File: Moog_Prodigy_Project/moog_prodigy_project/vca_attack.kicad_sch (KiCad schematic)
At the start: 14 parts, among them U105 MC14007UBCP, U106 MC14007UBCP, U107 MC14007UBCP

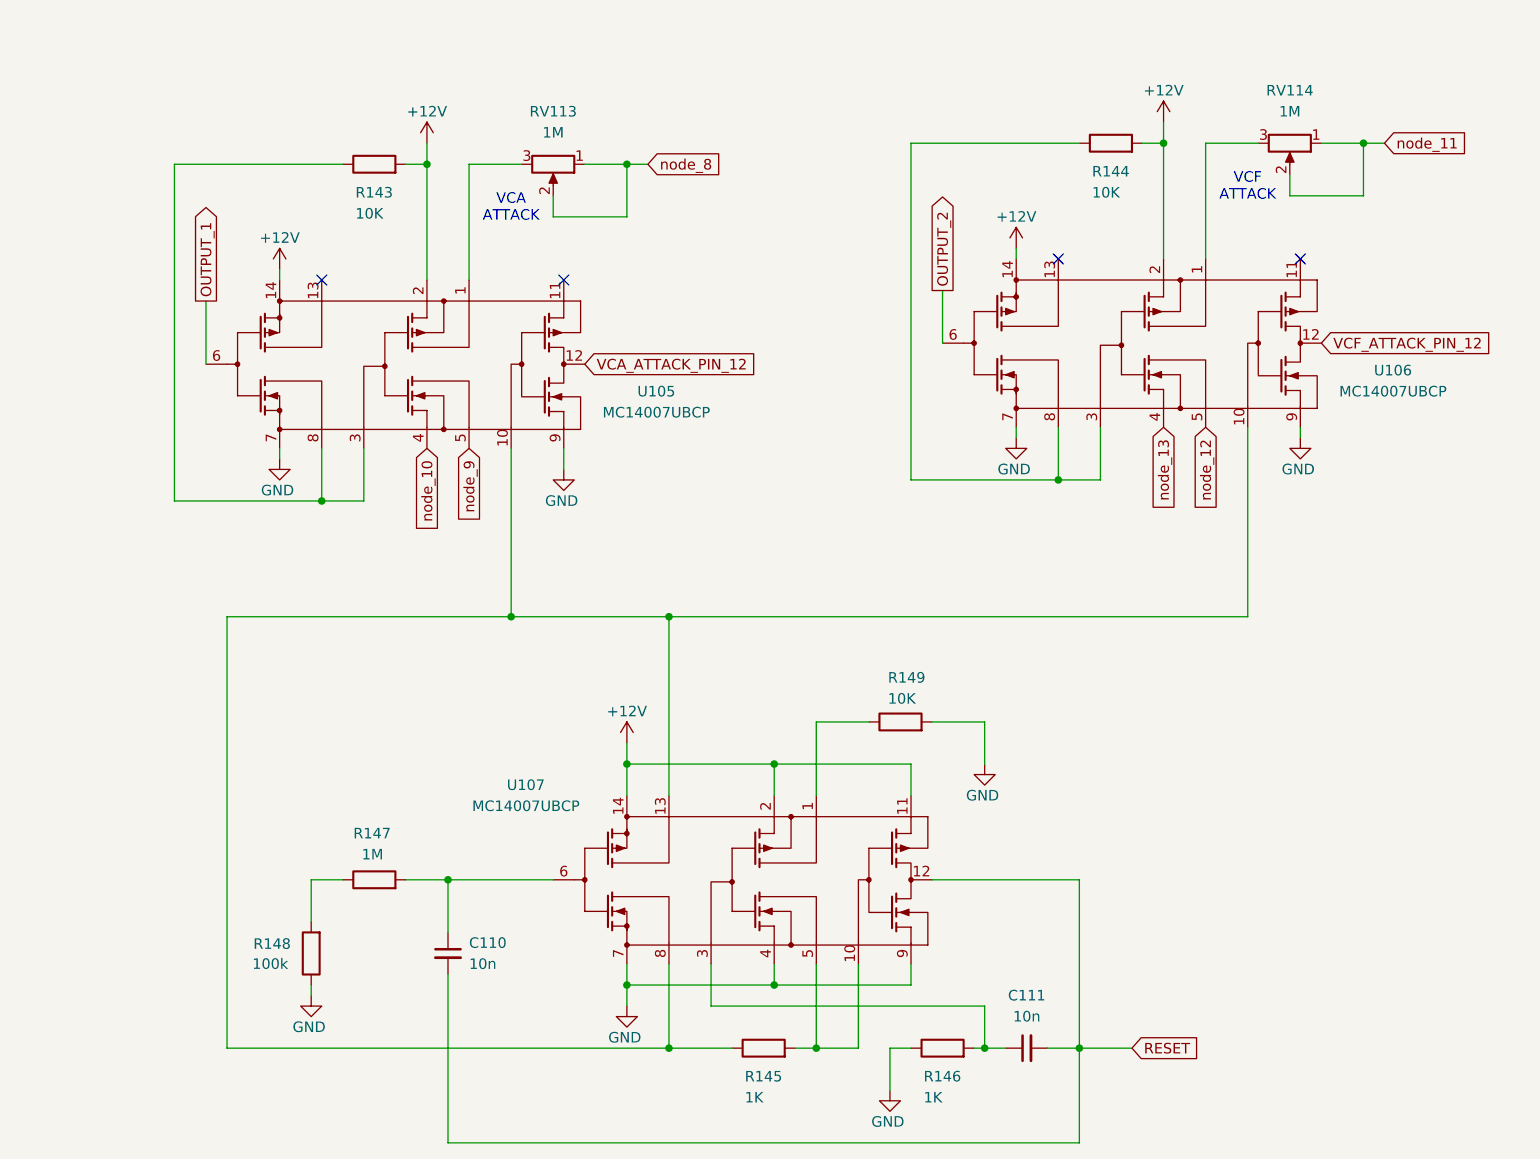
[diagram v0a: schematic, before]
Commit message: problemi sa ca3096, multiplicirani footprintovi
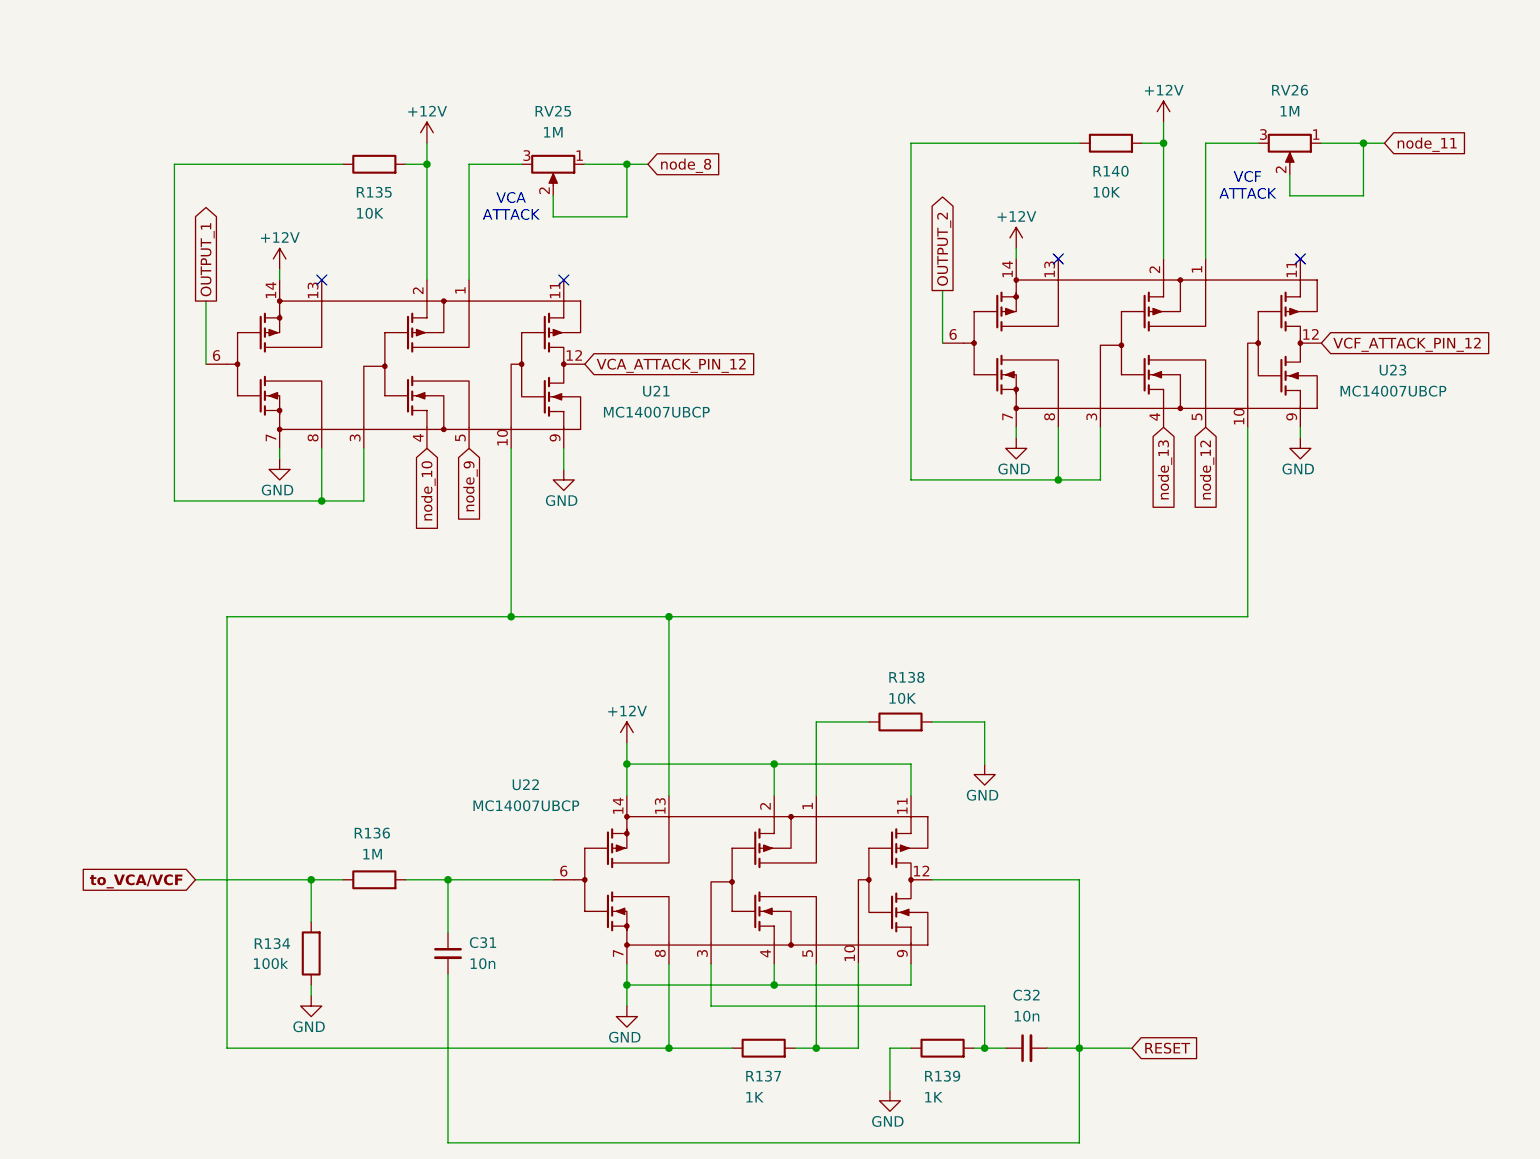
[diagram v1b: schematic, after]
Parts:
- renumbered C110 to C31, C111 to C32, R148 to R134, R143 to R135, R147 to R136, R145 to R137, R149 to R138, R146 to R139, R144 to R140, RV113 to RV25, RV114 to RV26, U105 to U21, U107 to U22, U106 to U23
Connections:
- net to_VCA/VCF: now reaches R134.2, R136.1
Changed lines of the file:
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@@
+	)
+	(junction
+		(at 74.93 125.73)
+		(diameter 0)
+		(color 0 0 0 0)
 	)
 	(junction
@@
 		(pts
 			(xy 156.21 111.76) (xy 156.21 106.68)
+		)
+		(stroke
+			(width 0)
+			(type default)
+		)
+	)
+	(wire
+		(pts
+			(xy 60.96 125.73) (xy 74.93 125.73)
 		)
 		(stroke
@@
 				)
 				(justify left)
+				(hide yes)
+			)
+		)
+	)
+	(global_label "to_VCA{slash}VCF"
+		(shape input)
+		(at 60.96 125.73 180)
+		(fields_autoplaced yes)
+		(effects
+			(font
+				(size 1.27 1.27)
+				(thickness 0.254)
+				(bold yes)
+			)
+			(justify right)
+		)
+		(property "Intersheetrefs" "${INTERSHEET_REFS}"
+			(at 46.4316 125.73 0)
+			(effects
+				(font
+					(size 1.27 1.27)
+				)
+				(justify right)
 				(hide yes)
 			)
@@
 		(on_board yes)
 		(dnp no)
-		(property "Reference" "R149"
+		(property "Reference" "R138"
 			(at 144.526 101.346 90)
 			(effects
@@
 			(project "moog_prodigy_project"
 				(path "/db469bdb-b6c3-4a16-9199-d4e6b8d556e8/f72090f0-21a5-4951-9fe6-dcdfafa76d53"
-					(reference "R149")
+					(reference "R138")
 					(unit 1)
 				)
@@
 		(on_board yes)
 		(dnp no)
-		(property "Reference" "R146"
+		(property "Reference" "R139"
 			(at 148.844 149.479 90)
 			(effects
@@
 			(project "moog_prodigy_project"
 				(path "/db469bdb-b6c3-4a16-9199-d4e6b8d556e8/f72090f0-21a5-4951-9fe6-dcdfafa76d53"
-					(reference "R146")
+					(reference "R139")
 					(unit 1)
 				)
@@
 		(on_board yes)
 		(dnp no)
-		(property "Reference" "#PWR0154"
+		(property "Reference" "#PWR0164"
 			(at 74.93 146.05 0)
 			(effects
@@
 			(project "moog_prodigy_project"
 				(path "/db469bdb-b6c3-4a16-9199-d4e6b8d556e8/f72090f0-21a5-4951-9fe6-dcdfafa76d53"
-					(reference "#PWR0154")
+					(reference "#PWR0164")
 					(unit 1)
 				)
@@
 		(on_board yes)
 		(dnp no)
-		(property "Reference" "U107"
+		(property "Reference" "U22"
 			(at 100.838 114.3 0)
 			(effects
@@
 			(project "moog_prodigy_project"
 				(path "/db469bdb-b6c3-4a16-9199-d4e6b8d556e8/f72090f0-21a5-4951-9fe6-dcdfafa76d53"
-					(reference "U107")
+					(reference "U22")
 					(unit 1)
 				)
@@
 		(on_board yes)
 		(dnp no)
-		(property "Reference" "#PWR0147"
+		(property "Reference" "#PWR0165"
 			(at 88.9 40.64 0)
 			(effects
@@
 			(project "moog_prodigy_project"
 				(path "/db469bdb-b6c3-4a16-9199-d4e6b8d556e8/f72090f0-21a5-4951-9fe6-dcdfafa76d53"
-					(reference "#PWR0147")
+					(reference "#PWR0165")
 					(unit 1)
 				)
@@
 		(on_board yes)
 		(dnp no)
-		(property "Reference" "R145"
+		(property "Reference" "R137"
 			(at 127.254 149.479 90)
 			(effects
@@
 			(project "moog_prodigy_project"
 				(path "/db469bdb-b6c3-4a16-9199-d4e6b8d556e8/f72090f0-21a5-4951-9fe6-dcdfafa76d53"
-					(reference "R145")
+					(reference "R137")
 					(unit 1)
 				)
@@
 		(on_board yes)
 		(dnp no)
-		(property "Reference" "#PWR0157"
+		(property "Reference" "#PWR0168"
 			(at 113.03 147.32 0)
 			(effects
@@
 			(project "moog_prodigy_project"
 				(path "/db469bdb-b6c3-4a16-9199-d4e6b8d556e8/f72090f0-21a5-4951-9fe6-dcdfafa76d53"
-					(reference "#PWR0157")
+					(reference "#PWR0168")
 					(unit 1)
 				)
@@
 		(on_board yes)
 		(dnp no)
-		(property "Reference" "R144"
+		(property "Reference" "R140"
 			(at 169.164 40.259 90)
 			(effects
@@
 			(project "moog_prodigy_project"
 				(path "/db469bdb-b6c3-4a16-9199-d4e6b8d556e8/f72090f0-21a5-4951-9fe6-dcdfafa76d53"
-					(reference "R144")
+					(reference "R140")
 					(unit 1)
 				)
@@
 		(dnp no)
 		(fields_autoplaced yes)
-		(property "Reference" "RV114"
+		(property "Reference" "RV26"
 			(at 193.04 30.48 90)
 			(effects
@@
 			(project "moog_prodigy_project"
 				(path "/db469bdb-b6c3-4a16-9199-d4e6b8d556e8/f72090f0-21a5-4951-9fe6-dcdfafa76d53"
-					(reference "RV114")
+					(reference "RV26")
 					(unit 1)
 				)
@@
 		(on_board yes)
 		(dnp no)
-		(property "Reference" "#PWR0152"
+		(property "Reference" "#PWR0172"
 			(at 160.02 78.74 0)
 			(effects
@@
 			(project "moog_prodigy_project"
 				(path "/db469bdb-b6c3-4a16-9199-d4e6b8d556e8/f72090f0-21a5-4951-9fe6-dcdfafa76d53"
-					(reference "#PWR0152")
+					(reference "#PWR0172")
 					(unit 1)
 				)
@@
 		(on_board yes)
 		(dnp no)
-		(property "Reference" "U105"
+		(property "Reference" "U21"
 			(at 116.586 66.802 0)
 			(effects
@@
 			(project "moog_prodigy_project"
 				(path "/db469bdb-b6c3-4a16-9199-d4e6b8d556e8/f72090f0-21a5-4951-9fe6-dcdfafa76d53"
-					(reference "U105")
+					(reference "U21")
 					(unit 1)
 				)
@@
 		(on_board yes)
 		(dnp no)
-		(property "Reference" "R147"
+		(property "Reference" "R136"
 			(at 80.01 120.142 90)
 			(effects
@@
 			(project "moog_prodigy_project"
 				(path "/db469bdb-b6c3-4a16-9199-d4e6b8d556e8/f72090f0-21a5-4951-9fe6-dcdfafa76d53"
-					(reference "R147")
+					(reference "R136")
 					(unit 1)
 				)
@@
 		(on_board yes)
 		(dnp no)
-		(property "Reference" "#PWR0151"
+		(property "Reference" "#PWR0166"
 			(at 105.41 82.55 0)
 			(effects
@@
 			(project "moog_prodigy_project"
 				(path "/db469bdb-b6c3-4a16-9199-d4e6b8d556e8/f72090f0-21a5-4951-9fe6-dcdfafa76d53"
-					(reference "#PWR0151")
+					(reference "#PWR0166")
 					(unit 1)
 				)
@@
 		(on_board yes)
 		(dnp no)
-		(property "Reference" "#PWR0155"
+		(property "Reference" "#PWR0167"
 			(at 113.03 113.03 0)
 			(effects
@@
 			(project "moog_prodigy_project"
 				(path "/db469bdb-b6c3-4a16-9199-d4e6b8d556e8/f72090f0-21a5-4951-9fe6-dcdfafa76d53"
-					(reference "#PWR0155")
+					(reference "#PWR0167")
 					(unit 1)
 				)
@@
 		(on_board yes)
 		(dnp no)
-		(property "Reference" "R143"
+		(property "Reference" "R135"
 			(at 80.264 42.799 90)
 			(effects
@@
 			(project "moog_prodigy_project"
 				(path "/db469bdb-b6c3-4a16-9199-d4e6b8d556e8/f72090f0-21a5-4951-9fe6-dcdfafa76d53"
-					(reference "R143")
+					(reference "R135")
 					(unit 1)
 				)
@@
 		(dnp no)
 		(fields_autoplaced yes)
-		(property "Reference" "C111"
+		(property "Reference" "C32"
 			(at 161.2963 139.7 90)
 			(effects
@@
 			(project "moog_prodigy_project"
 				(path "/db469bdb-b6c3-4a16-9199-d4e6b8d556e8/f72090f0-21a5-4951-9fe6-dcdfafa76d53"
-					(reference "C111")
+					(reference "C32")
 					(unit 1)
 				)
@@
 		(dnp no)
 		(fields_autoplaced yes)
-		(property "Reference" "RV113"
+		(property "Reference" "RV25"
 			(at 104.14 33.02 90)
 			(effects
@@
 			(project "moog_prodigy_project"
 				(path "/db469bdb-b6c3-4a16-9199-d4e6b8d556e8/f72090f0-21a5-4951-9fe6-dcdfafa76d53"
-					(reference "RV113")
+					(reference "RV25")
 					(unit 1)
 				)
@@
 		(on_board yes)
 		(dnp no)
-		(property "Reference" "U106"
+		(property "Reference" "U23"
 			(at 205.486 64.262 0)
 			(effects
@@
 			(project "moog_prodigy_project"
 				(path "/db469bdb-b6c3-4a16-9199-d4e6b8d556e8/f72090f0-21a5-4951-9fe6-dcdfafa76d53"
-					(reference "U106")
+					(reference "U23")
 					(unit 1)
 				)
@@
 		(on_board yes)
 		(dnp no)
-		(property "Reference" "#PWR0149"
+		(property "Reference" "#PWR0173"
 			(at 177.8 38.1 0)
 			(effects
@@
 			(project "moog_prodigy_project"
 				(path "/db469bdb-b6c3-4a16-9199-d4e6b8d556e8/f72090f0-21a5-4951-9fe6-dcdfafa76d53"
-					(reference "#PWR0149")
+					(reference "#PWR0173")
 					(unit 1)
 				)
@@
 		(on_board yes)
 		(dnp no)
-		(property "Reference" "R148"
+		(property "Reference" "R134"
 			(at 67.945 133.477 0)
 			(effects
@@
 			(project "moog_prodigy_project"
 				(path "/db469bdb-b6c3-4a16-9199-d4e6b8d556e8/f72090f0-21a5-4951-9fe6-dcdfafa76d53"
-					(reference "R148")
+					(reference "R134")
 					(unit 1)
 				)
@@
 		(on_board yes)
 		(dnp no)
-		(property "Reference" "#PWR0153"
+		(property "Reference" "#PWR0174"
 			(at 194.31 78.74 0)
 			(effects
@@
 			(project "moog_prodigy_project"
 				(path "/db469bdb-b6c3-4a16-9199-d4e6b8d556e8/f72090f0-21a5-4951-9fe6-dcdfafa76d53"
-					(reference "#PWR0153")
+					(reference "#PWR0174")
 					(unit 1)
 				)
@@
 		(on_board yes)
 		(dnp no)
-		(property "Reference" "#PWR0146"
+		(property "Reference" "#PWR0162"
 			(at 71.12 55.88 0)
 			(effects
@@
 			(project "moog_prodigy_project"
 				(path "/db469bdb-b6c3-4a16-9199-d4e6b8d556e8/f72090f0-21a5-4951-9fe6-dcdfafa76d53"
-					(reference "#PWR0146")
+					(reference "#PWR0162")
 					(unit 1)
 				)
@@
 		(on_board yes)
 		(dnp no)
-		(property "Reference" "#PWR0156"
+		(property "Reference" "#PWR0170"
 			(at 156.21 118.11 0)
 			(effects
@@
 			(project "moog_prodigy_project"
 				(path "/db469bdb-b6c3-4a16-9199-d4e6b8d556e8/f72090f0-21a5-4951-9fe6-dcdfafa76d53"
-					(reference "#PWR0156")
+					(reference "#PWR0170")
 					(unit 1)
 				)
@@
 		(on_board yes)
 		(dnp no)
-		(property "Reference" "#PWR0158"
+		(property "Reference" "#PWR0169"
 			(at 144.78 157.48 0)
 			(effects
@@
 			(project "moog_prodigy_project"
 				(path "/db469bdb-b6c3-4a16-9199-d4e6b8d556e8/f72090f0-21a5-4951-9fe6-dcdfafa76d53"
-					(reference "#PWR0158")
+					(reference "#PWR0169")
 					(unit 1)
 				)
@@
 		(dnp no)
 		(fields_autoplaced yes)
-		(property "Reference" "C110"
+		(property "Reference" "C31"
 			(at 93.98 133.3562 0)
 			(effects
@@
 			(project "moog_prodigy_project"
 				(path "/db469bdb-b6c3-4a16-9199-d4e6b8d556e8/f72090f0-21a5-4951-9fe6-dcdfafa76d53"
-					(reference "C110")
+					(reference "C31")
 					(unit 1)
 				)
@@
 		(on_board yes)
 		(dnp no)
-		(property "Reference" "#PWR0148"
+		(property "Reference" "#PWR0171"
 			(at 160.02 53.34 0)
 			(effects
@@
 			(project "moog_prodigy_project"
 				(path "/db469bdb-b6c3-4a16-9199-d4e6b8d556e8/f72090f0-21a5-4951-9fe6-dcdfafa76d53"
-					(reference "#PWR0148")
+					(reference "#PWR0171")
 					(unit 1)
 				)
@@
 		(on_board yes)
 		(dnp no)
-		(property "Reference" "#PWR0150"
+		(property "Reference" "#PWR0163"
 			(at 71.12 81.28 0)
 			(effects
@@
 			(project "moog_prodigy_project"
 				(path "/db469bdb-b6c3-4a16-9199-d4e6b8d556e8/f72090f0-21a5-4951-9fe6-dcdfafa76d53"
-					(reference "#PWR0150")
+					(reference "#PWR0163")
 					(unit 1)
 				)

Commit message: Fix 1 nakon review-a 27.05.2026
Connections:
- net +12V: now also U21., U22., U23.; no longer U21.14, U21.2, U22.11, U22.14, U22.2, U23.14, U23.2
- net GND: now also U21., U22., U23.; no longer U21.7, U21.9, U22.4, U22.7, U22.9, U23.7, U23.9
- net OUTPUT_1: now also U21.; no longer U21.6
- net OUTPUT_2: now also U23.; no longer U23.6
- net RESET: now also U22.; no longer U22.12
- net VCA_ATTACK_PIN_12: now also U21.; no longer U21.12
- net VCF_ATTACK_PIN_12: now also U23.; no longer U23.12
- net node_10: now also U21.; no longer U21.4
- net node_12: now also U23.; no longer U23.5
- net node_13: now also U23.; no longer U23.4
- net node_9: now also U21.; no longer U21.5
- net at R138.1: now also U22.; no longer U22.1
- net at C32.1, R139.2: now also U22.; no longer U22.3
- net at C31.1, R136.2: now also U22.; no longer U22.6
- net at RV26.3: now also U23.; no longer U23.1
- net at RV25.3: now also U21.; no longer U21.1
- new net: R137.1, U21., U22., U23.
- new net: R137.2, U22.
- new net: R140.1, U23.
- new net: R135.1, U21.
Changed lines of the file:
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@@
 	(generator_version "9.0")
 	(paper "A4")
+	(title_block
+		(rev "Marjan Urekar")
+		(comment 1 "Fakultet tehničkih nauka")
+		(comment 2 "Univerzitet u Novom Sadu")
+		(comment 3 "Merno-Informacioni sistemi")
+	)
 	(text "VCF\nATTACK"
 		(exclude_from_sim no)
@@
 			)
 		)
-		(pin "14"
-		)
-		(pin "10"
-		)
-		(pin "6"
-		)
-		(pin "3"
-		)
-		(pin "12"
-		)
-		(pin "8"
-		)
-		(pin "4"
-		)
-		(pin "1"
-		)
-		(pin "7"
-		)
-		(pin "13"
-		)
-		(pin "2"
-		)
-		(pin "11"
-		)
-		(pin "9"
-		)
-		(pin "5"
+		(pin ""
+		)
+		(pin ""
+		)
+		(pin ""
+		)
+		(pin ""
+		)
+		(pin ""
+		)
+		(pin ""
+		)
+		(pin ""
+		)
+		(pin ""
+		)
+		(pin ""
+		)
+		(pin ""
+		)
+		(pin ""
+		)
+		(pin ""
+		)
+		(pin ""
+		)
+		(pin ""
 		)
 		(instances
@@
 			)
 		)
-		(pin "14"
-		)
-		(pin "10"
-		)
-		(pin "6"
-		)
-		(pin "3"
-		)
-		(pin "12"
-		)
-		(pin "8"
-		)
-		(pin "4"
-		)
-		(pin "1"
-		)
-		(pin "7"
-		)
-		(pin "13"
-		)
-		(pin "2"
-		)
-		(pin "11"
-		)
-		(pin "9"
-		)
-		(pin "5"
+		(pin ""
+		)
+		(pin ""
+		)
+		(pin ""
+		)
+		(pin ""
+		)
+		(pin ""
+		)
+		(pin ""
+		)
+		(pin ""
+		)
+		(pin ""
+		)
+		(pin ""
+		)
+		(pin ""
+		)
+		(pin ""
+		)
+		(pin ""
+		)
+		(pin ""
+		)
+		(pin ""
 		)
 		(instances
@@
 			)
 		)
-		(pin "14"
-		)
-		(pin "10"
-		)
-		(pin "6"
-		)
-		(pin "3"
-		)
-		(pin "12"
-		)
-		(pin "8"
-		)
-		(pin "4"
-		)
-		(pin "1"
-		)
-		(pin "7"
-		)
-		(pin "13"
-		)
-		(pin "2"
-		)
-		(pin "11"
-		)
-		(pin "9"
-		)
-		(pin "5"
+		(pin ""
+		)
+		(pin ""
+		)
+		(pin ""
+		)
+		(pin ""
+		)
+		(pin ""
+		)
+		(pin ""
+		)
+		(pin ""
+		)
+		(pin ""
+		)
+		(pin ""
+		)
+		(pin ""
+		)
+		(pin ""
+		)
+		(pin ""
+		)
+		(pin ""
+		)
+		(pin ""
 		)
 		(instances

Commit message: Latest checkpoints update 05.06.2026
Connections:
- new net: R137.1, U21., U22., U23.
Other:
- moved on the sheet: C31, C32, R134, R135, R136, R137, R138, R139, R140, RV25, RV26, U21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

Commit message: 27.06.2026 - dodavanje izmena sa konsultacija
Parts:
- R134: value 100k -> 100K
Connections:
- new net: R137.1, U21., U22., U23.
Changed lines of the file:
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@@
 		(comment 1 "Fakultet tehničkih nauka")
 		(comment 2 "Univerzitet u Novom Sadu")
-		(comment 3 "Merno-Informacioni sistemi")
+		(comment 3 "Merno-Informacioni sistemi ")
 	)
 	(text "VCF\nATTACK"
@@
 			)
 		)
-		(property "Value" "100k"
+		(property "Value" "100K"
 			(at 63.246 127.508 0)
 			(effects
